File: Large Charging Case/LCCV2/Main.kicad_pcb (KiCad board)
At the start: 2 copper layers, 136.2 x 62.1 mm, 258 parts, among them J1 Conn_02x05_Odd_Even, J10 Coil A, J11 Coil B, J12 TX_Coil, J13 Coil A, J14 Coil B, J15 TX_Coil, J16 Coil A, J17 Coil B, J18 TX_Coil, J19 Coil A, J2 Coil B, J20 Coil B, J21 TX_Coil, J22 Coil A, J23 USB_C_Receptacle_USB2.0, J24 Conn_01x02, J25 Coil B, J26 TX_Coil, J27 Coil A, J3 TX_Coil, J4 Coil A, J5 Coil B, J6 TX_Coil, J7 Coil A, J8 Coil B, J9 TX_Coil, P1 heard4, SW1 SW_Push, U1 N52810_QFN32, U10 XKT001, U11 XKT335, U12 XKT001, U13 XKT335, U14 XKT001, U15 XKT335, U16 LP78071, U17 74HC4051PW, U18 LM2902, U19 74HCT259, U2 XKT001, U20 LM2902, U22 LN3406, U23 XKT001, U24 XKT335, U3 XKT335, U4 XKT001, U5 XKT335, U6 XKT001, U7 XKT335, U8 XKT001, U9 XKT335, Y1 32MHz 40ppm

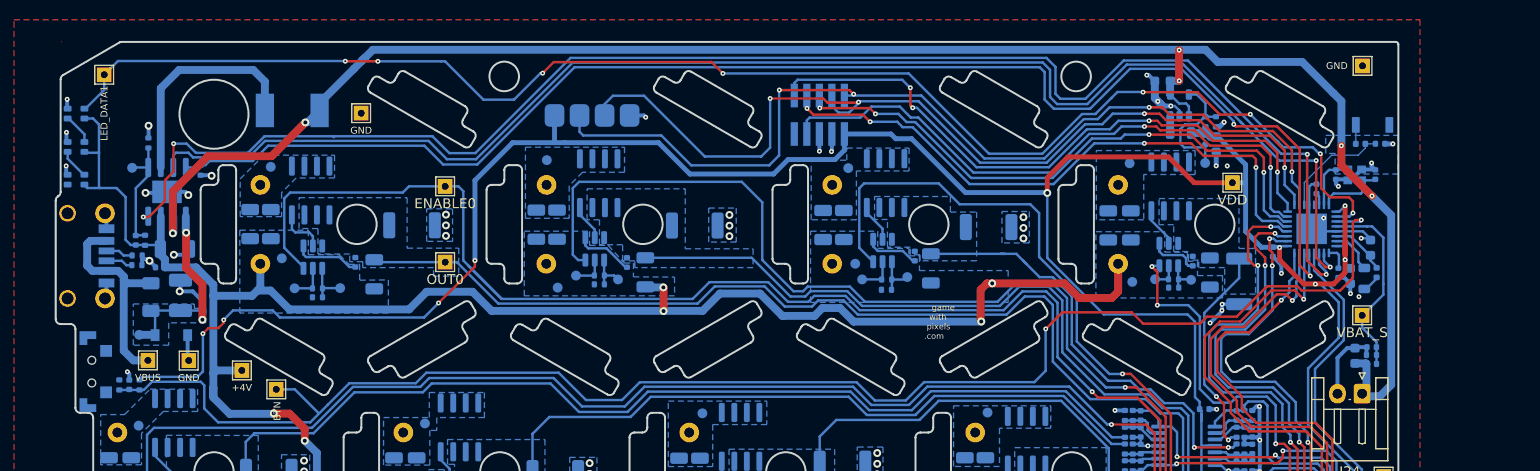
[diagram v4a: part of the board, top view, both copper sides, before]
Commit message: Better RF Path and edge component placements
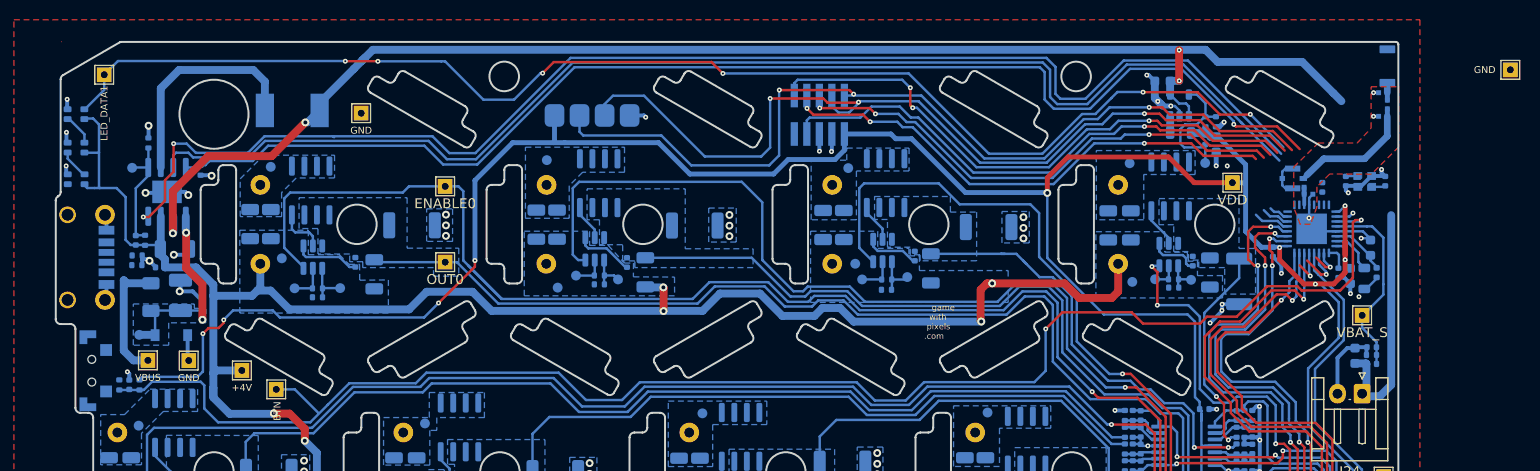
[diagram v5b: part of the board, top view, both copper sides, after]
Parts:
- added C73: DNP, Pixels-dice:0402_RF, B.Cu at (210.9, 63.9)
- added C9: 0.8pF 10V 5% NP0, Pixels-dice:0402_RF, B.Cu at (203.4, 74.2)
- added J28: DNP, RFFrontEnd:MFH3.RECE.20369.001E.01, B.Cu at (201.8, 72.6)
- added L6: 3.9nH 5%, Pixels-dice:0402_RF, B.Cu at (202.9, 73.0)
- AE1: value ChipAnt -> Antenna_Chip
- C8: value 0.8pF 10V NP0 -> 0.8pF 10V 5% NP0; footprint Capacitor_SMD:C_0402_1005Metric -> Pixels-dice:0402_RF
- L3: value 3.9nH -> 1.5nH 5%; footprint Inductor_SMD:L_0402_1005Metric -> Pixels-dice:0402_RF
- moved W44 15.0 mm to (223.9, 61.6)
- moved AE1 5.34 mm to (211.4, 62.9), turned to 180 degrees
- moved L3 4.83 mm to (211.4, 65.1), turned to 90 degrees
- moved C8 2.79 mm to (210.9, 66.3)
- moved C5 1.21 mm to (211.2, 72.9)
- moved C6 1.21 mm to (207.2, 72.9)
- moved Y1 1.21 mm to (209.1, 72.9)
- moved C7 0.61 mm to (204.8, 73.5)
- moved J23 0.15 mm to (79.4, 80.6)
- moved SW1 0.09 mm to (80.0, 92.1)
- moved D2 0.07 mm to (78.4, 69.5)
- moved D3 0.06 mm to (78.4, 66.1)
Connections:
- net /ANT_CHIP renamed /ANTENNA
- AE1 pad 2: (no net) -> unconnected-(AE1-Pad2)
- C8 pad 1: GND -> /ANT_50
- C8 pad 2: /ANT_NRF -> GND
- L3 pad 1: /ANT_NRF -> /ANT_50
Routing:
- net +BATT: track 181.0 -> 167.4 mm, vias 6 -> 4
- net /Power/CHARGE: track 146.0 -> 132.5 mm, vias 2 -> 1
- net /Power/4V_EN: track 155.1 -> 141.7 mm, vias 4 -> 3
- net /ANT_50: track 0.00 -> 13.1 mm
- net Net-(D3-Pad1): track 150.9 -> 138.4 mm, vias 8 -> 7
- net /Power/BAT_I_SENSE: track 143.1 -> 131.3 mm
- net /ANT_NRF: track 11.4 -> 1.79 mm
- net VBUS: track 21.7 -> 12.9 mm
- net RESET: track 64.8 -> 58.4 mm, vias 4 -> 3
- net SWDCLK: track 95.0 -> 89.3 mm, vias 4 -> 3
- net SWDIO: track 95.8 -> 90.1 mm, vias 4 -> 3
- net TXO: track 60.4 -> 54.8 mm, vias 4 -> 3
- net Net-(C5-Pad2): track 6.99 -> 1.42 mm
- net RXI: track 62.4 -> 57.0 mm, vias 2 -> 1
- net SWO: track 59.0 -> 53.7 mm, vias 4 -> 3
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
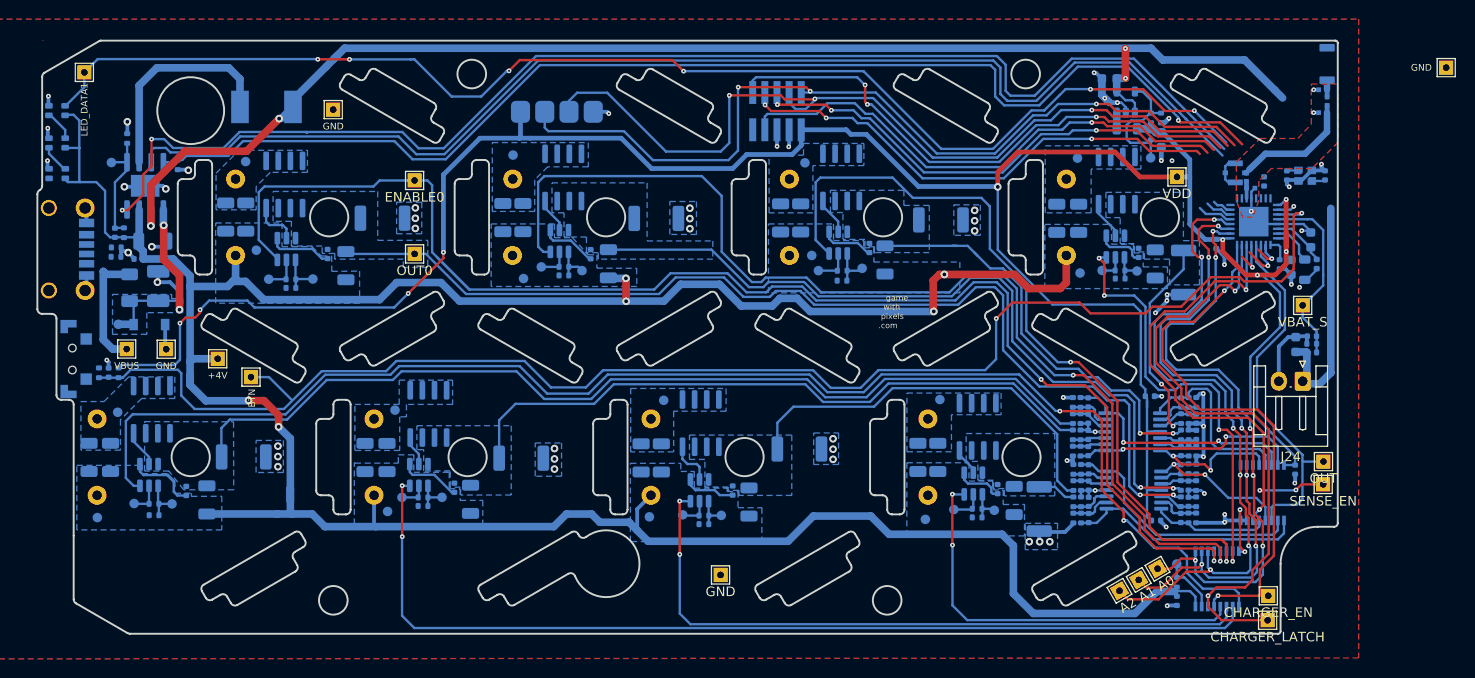
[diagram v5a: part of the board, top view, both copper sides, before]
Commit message: LCCV2 Update from Wang Qing and Me. Moved connector, improved antenna layout.
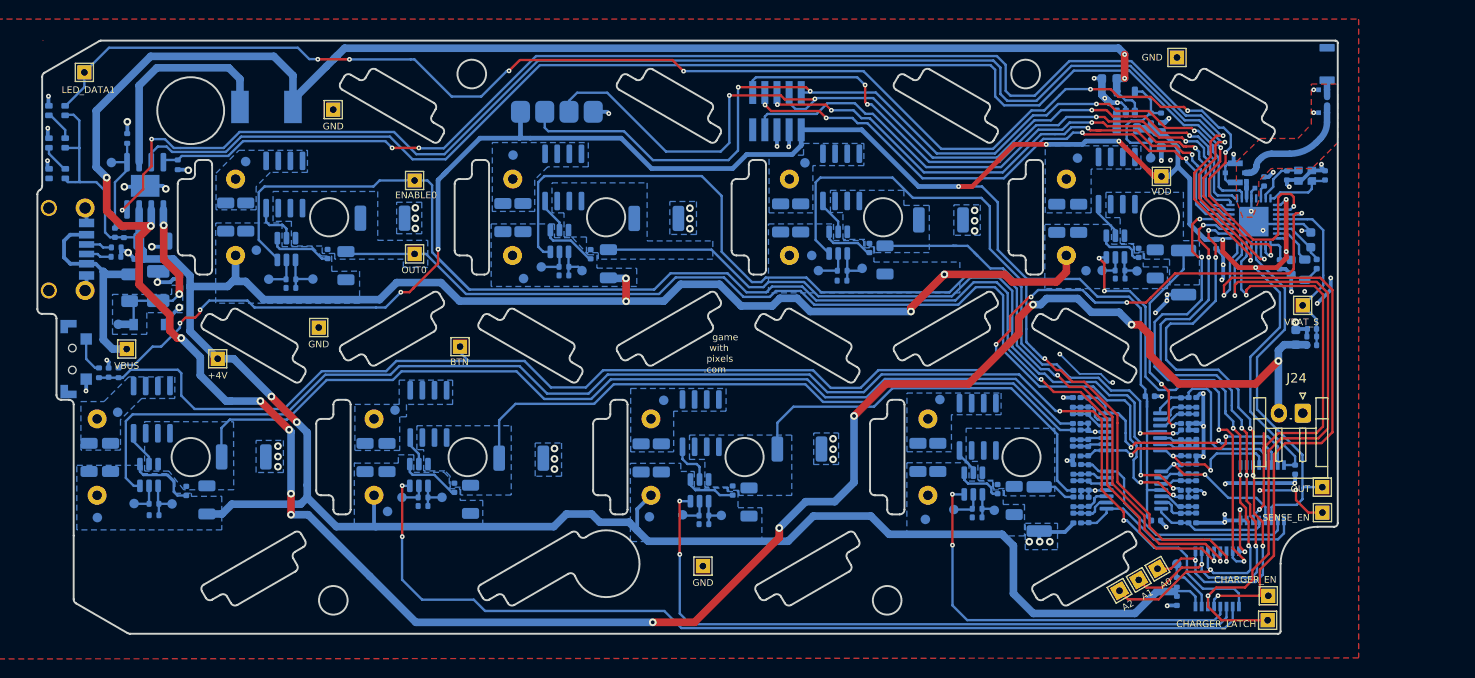
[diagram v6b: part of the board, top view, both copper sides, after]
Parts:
- moved J9 265.6 mm to (193.9, 77.3)
- moved J26 265.1 mm to (179.4, 102.4)
- moved J6 264.6 mm to (164.9, 77.3)
- moved J15 264.1 mm to (150.4, 102.4)
- moved J3 263.6 mm to (135.9, 77.3)
- moved J18 263.1 mm to (121.4, 102.4)
- moved J12 262.6 mm to (106.9, 77.3)
- moved J21 262.1 mm to (92.4, 102.4)
- moved W44 28.2 mm to (195.7, 60.5)
- moved W76 22.1 mm to (120.6, 90.8)
- moved W45 16.1 mm to (105.8, 88.8)
- moved J24 3.34 mm to (208.8, 97.8)
- moved W48 2.95 mm to (210.9, 108.2)
- moved W47 2.67 mm to (210.9, 105.5)
- moved W3 2.06 mm to (146.0, 113.8)
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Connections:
- J24 pad 1: +BATT -> GND
- J24 pad 2: GND -> +BATT
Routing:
- net +BATT: track 167.4 -> 327.1 mm, vias 4 -> 15
- net Net-(D3-Pad1): track 138.4 -> 162.7 mm, vias 7 -> 8
- net GND: track 126.2 -> 143.7 mm, vias 69 -> 81
- net /Power/4V_EN: track 141.7 -> 154.4 mm, vias 3 -> 4
- net /Power/CHARGE: track 132.5 -> 145.1 mm, vias 1 -> 2
- net /Power/BAT_I_SENSE: track 131.3 -> 143.2 mm, vias 2 -> 4
- net +4V: track 355.5 -> 345.0 mm
- net VBUS: track 12.9 -> 22.0 mm
- net /Multiplexed Chargers/CHARGER_ENL_D: track 56.9 -> 63.2 mm
- net RESET: track 58.4 -> 64.6 mm, vias 3 -> 4
- net SWDCLK: track 89.3 -> 95.0 mm, vias 3 -> 4
- net SWDIO: track 90.1 -> 95.7 mm, vias 3 -> 4
- net Net-(C5-Pad2): track 1.42 -> 6.99 mm
- net SWO: track 53.7 -> 59.2 mm, vias 3 -> 4
- net TXO: track 54.8 -> 59.9 mm, vias 3 -> 4
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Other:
- board text added: "Pixels Large Charging Case V2.0"
- board text removed: "Pixels Large Charging Case V1"
